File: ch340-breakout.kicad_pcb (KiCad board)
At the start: 2 copper layers, 31.8 x 28.9 mm, 20 parts, among them J1 USB_B_Mini, J2 Conn_01x08_Male, J3 Conn_02x05_Odd_Even, U1 SPX3819M5-L-3-3, U2 USBLC6-2SC6, U3 CH340G, Y1 12Mhz

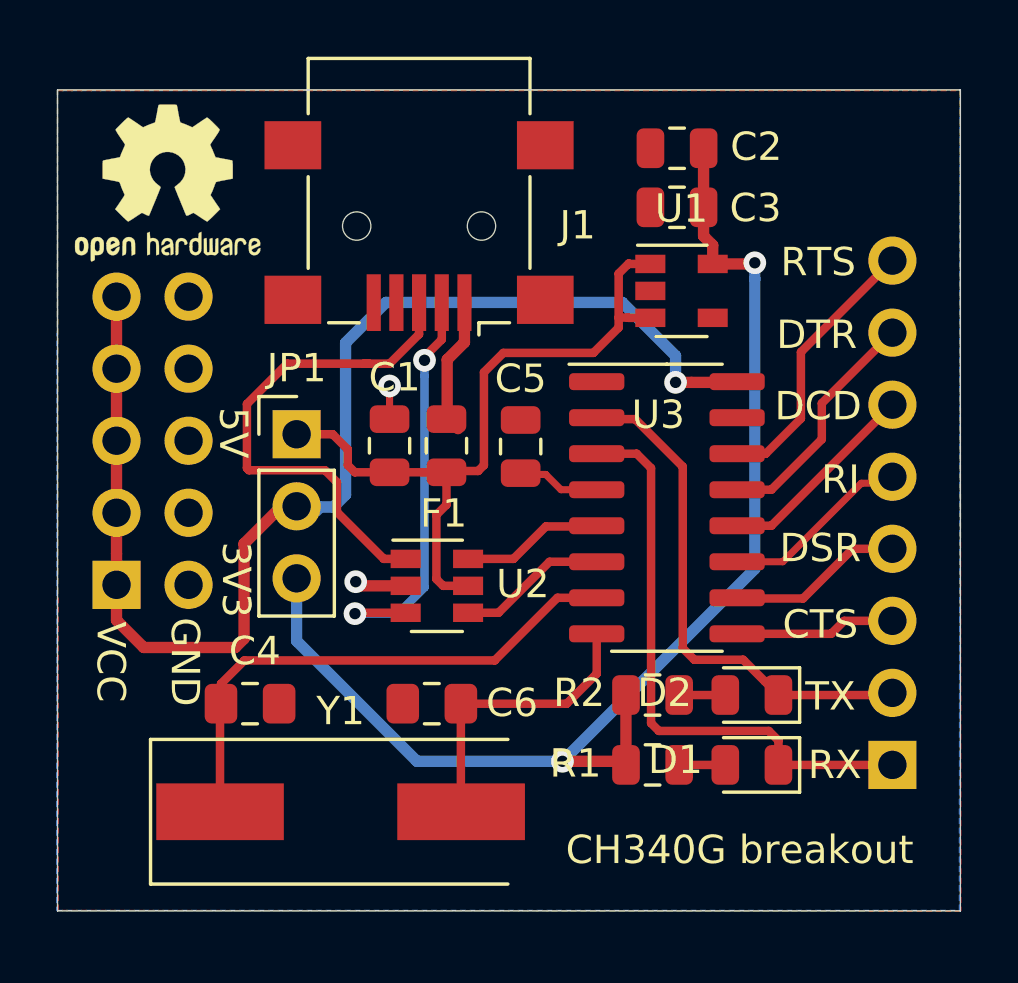
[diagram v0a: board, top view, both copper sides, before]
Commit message: finalizing and add power on led
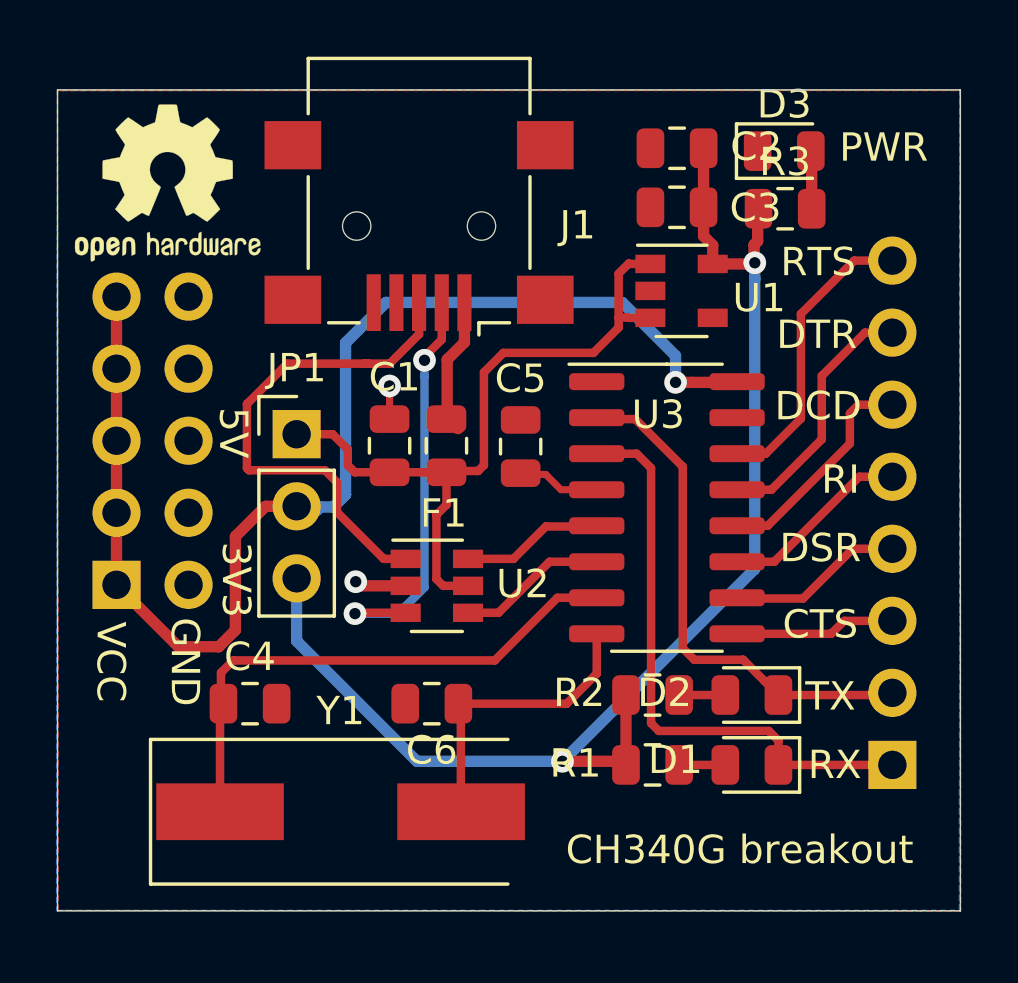
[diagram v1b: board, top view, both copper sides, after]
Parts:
- added D3: LED GREEN, LED_SMD:LED_0805_2012Metric, F.Cu at (166.3, 60.6)
- added R3: 100, Resistor_SMD:R_0805_2012Metric, F.Cu at (166.3, 62.6)
- C4, C6: footprint Capacitor_SMD:C_0805_2012Metric_Pad1.15x1.40mm_HandSolder -> Capacitor_SMD:C_0805_2012Metric
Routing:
- net Net-(D3-Pad2): track 0.00 -> 2.04 mm
- net +3V3: track 44.5 -> 46.5 mm
- net VCC: track 44.8 -> 43.8 mm
- net CH_RTS: track 9.67 -> 10.5 mm
- net CH_DCD: track 7.24 -> 7.87 mm
- net CH_DTR: track 7.88 -> 8.44 mm
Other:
- board text added: "$$version"
- board text added: "PWR"
- board text added: "https://820labs.net/ projects/ch340-breakout"

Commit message: silkscreen tweaks
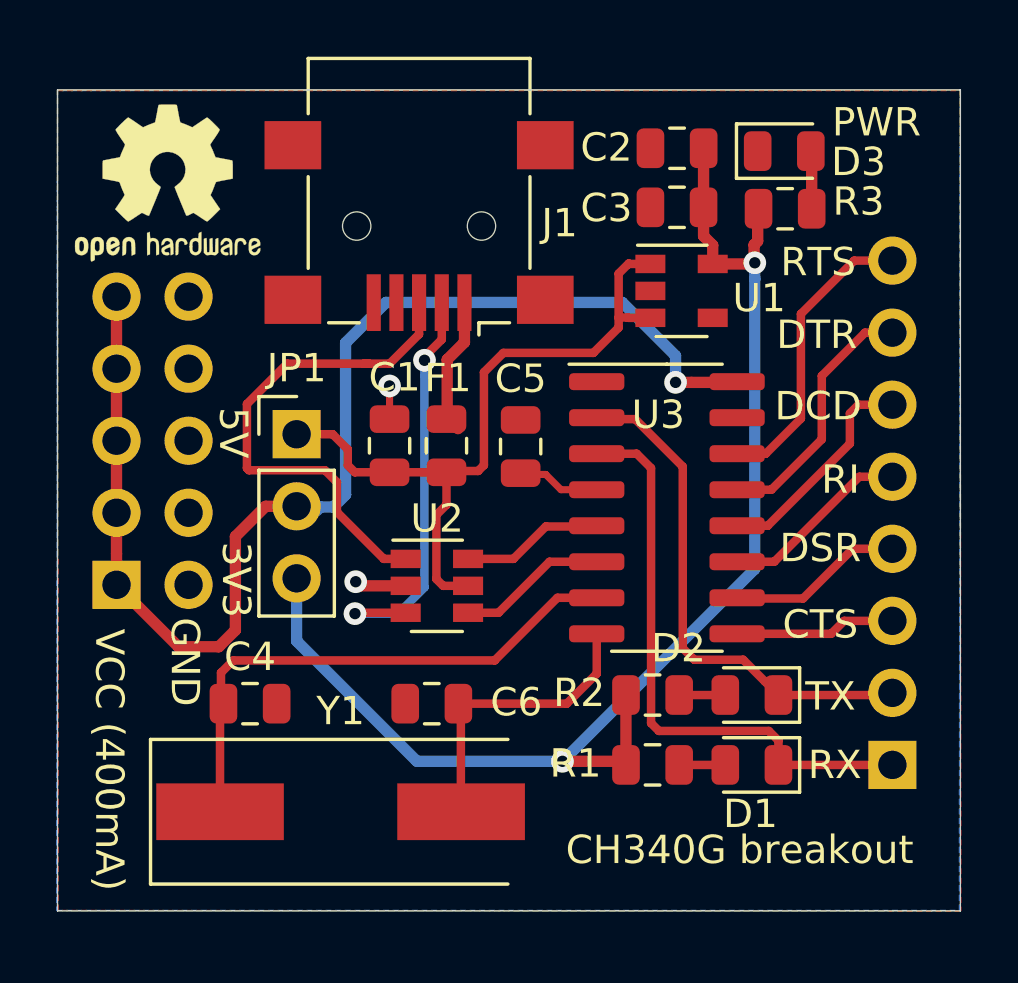
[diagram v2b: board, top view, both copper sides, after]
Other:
- board text added: "VCC (400mA)"
- board text removed: "VCC"
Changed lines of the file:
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@@
     (tags resistor)
     (attr smd)
-    (fp_text reference R3 (at 0 -1.65) (layer F.SilkS)
+    (fp_text reference R3 (at 2.5885 -0.254) (layer F.SilkS)
       (effects (font (size 1 1) (thickness 0.15)))
     )
@@
     (tags diode)
     (attr smd)
-    (fp_text reference D3 (at 0 -1.65) (layer F.SilkS)
+    (fp_text reference D3 (at 2.6185 0.381) (layer F.SilkS)
       (effects (font (size 1 1) (thickness 0.15)))
     )
@@
     (tags capacitor)
     (attr smd)
-    (fp_text reference C6 (at 0 -1.65) (layer F.SilkS)
+    (fp_text reference C6 (at -2.9808 0.0508) (layer F.SilkS)
       (effects (font (size 1 1) (thickness 0.15)))
     )
@@
     (tags resistor)
     (attr smd)
-    (fp_text reference F1 (at -2.3899 -0.1016 180) (layer F.SilkS)
+    (fp_text reference F1 (at 2.3853 0.0508 180) (layer F.SilkS)
       (effects (font (size 1 1) (thickness 0.15)))
     )
@@
     (tags capacitor)
     (attr smd)
-    (fp_text reference C3 (at -2.7686 -0.0254) (layer F.SilkS)
+    (fp_text reference C3 (at 2.4892 -0.0254) (layer F.SilkS)
       (effects (font (size 1 1) (thickness 0.15)))
     )
@@
     (tags capacitor)
     (attr smd)
-    (fp_text reference C2 (at -2.7917 0.0508) (layer F.SilkS)
+    (fp_text reference C2 (at 2.4915 0.0254) (layer F.SilkS)
       (effects (font (size 1 1) (thickness 0.15)))
     )
@@
     (tags SOT-23-6)
     (attr smd)
-    (fp_text reference U2 (at 3.0304 -0.061) (layer F.SilkS)
+    (fp_text reference U2 (at 0.0078 -2.3724) (layer F.SilkS)
       (effects (font (size 1 1) (thickness 0.15)))
     )
@@
     (tags "USB USB_B USB_Mini connector")
     (attr smd)
-    (fp_text reference J1 (at -5.588 0.0254) (layer F.SilkS)
+    (fp_text reference J1 (at -4.953 0.1016) (layer F.SilkS)
       (effects (font (size 1 1) (thickness 0.15)))
     )
@@
     (tags diode)
     (attr smd)
-    (fp_text reference D2 (at 3.0734 0.0762) (layer F.SilkS)
+    (fp_text reference D2 (at 2.5885 1.651) (layer F.SilkS)
       (effects (font (size 1 1) (thickness 0.15)))
     )
@@
     (tags diode)
     (attr smd)
-    (fp_text reference D1 (at 2.6947 0.1778) (layer F.SilkS)
+    (fp_text reference D1 (at 0.0485 -1.7272) (layer F.SilkS)
       (effects (font (size 1 1) (thickness 0.15)))
     )
@@
     )
   )
-  (gr_text PWR (at 169.799 60.452) (layer F.SilkS)
+  (gr_text PWR (at 169.545 59.563) (layer F.SilkS)
     (effects (font (size 1 1) (thickness 0.25)))
   )
@@
     (effects (font (size 1 1) (thickness 0.25)))
   )
-  (gr_text VCC (at 142.5448 78.5876 270) (layer F.SilkS)
+  (gr_text "VCC (400mA)" (at 142.494 82.042 270) (layer F.SilkS)
     (effects (font (size 1 1) (thickness 0.25)))
   )

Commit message: prepare for publishing: fixing LED resistor values, archive footprints, add missing data sheets
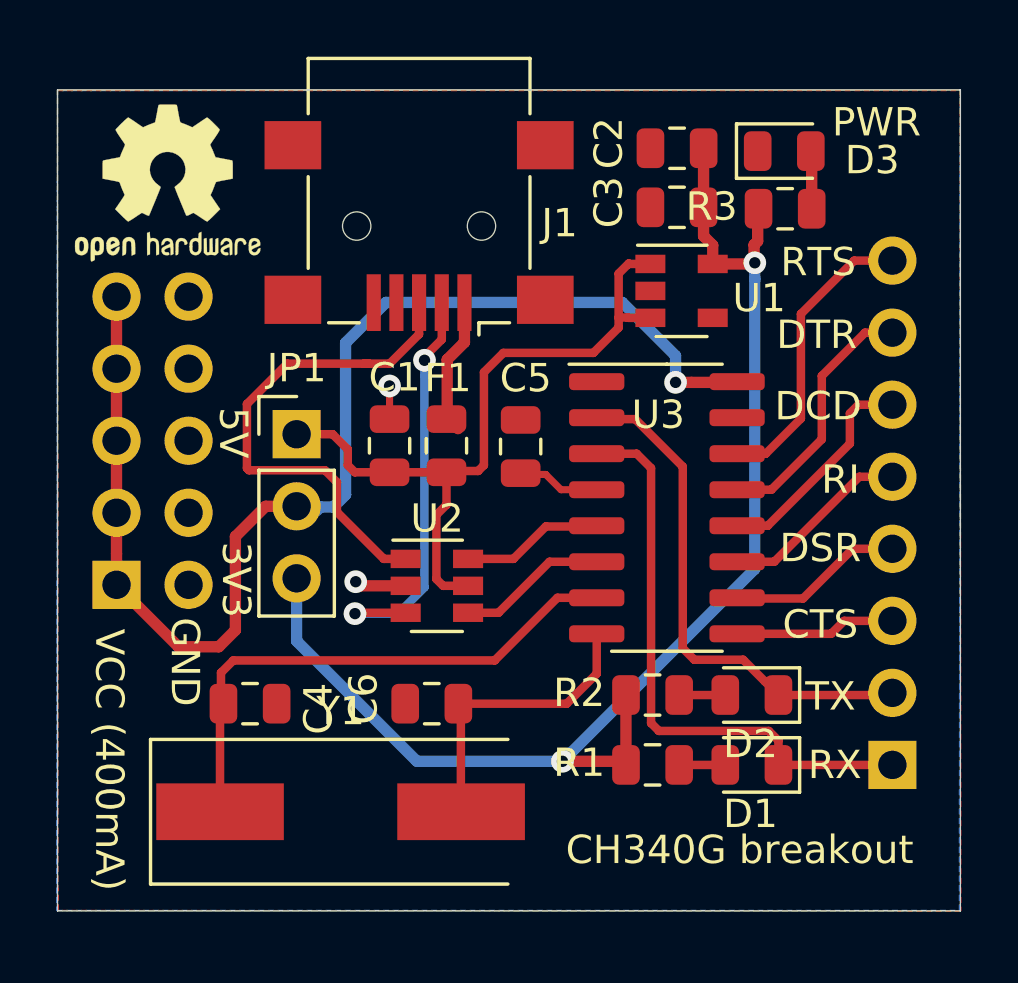
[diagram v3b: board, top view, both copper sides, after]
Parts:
- C1, C2, C3, C4, C5, C6: footprint Capacitor_SMD:C_0805_2012Metric -> ch340-breakout:C_0805_2012Metric
- D1, D2, D3: footprint LED_SMD:LED_0805_2012Metric -> ch340-breakout:LED_0805_2012Metric
- F1: footprint Fuse:Fuse_0805_2012Metric -> ch340-breakout:Fuse_0805_2012Metric
- J1: footprint Connector_USB:USB_Mini-B_Lumberg_2486_01_Horizontal -> ch340-breakout:USB_Mini-B_Lumberg_2486_01_Horizontal
- J2: footprint Connector_PinHeader_2.54mm:PinHeader_1x08_P2.54mm_Vertical -> ch340-breakout:PinHeader_1x08_P2.54mm_Vertical
- J3: footprint Connector_PinHeader_2.54mm:PinHeader_2x05_P2.54mm_Vertical -> ch340-breakout:PinHeader_2x05_P2.54mm_Vertical
- JP1: footprint Connector_PinHeader_2.54mm:PinHeader_1x03_P2.54mm_Vertical -> ch340-breakout:PinHeader_1x03_P2.54mm_Vertical
- R1, R3: value 100 -> 3K3; footprint Resistor_SMD:R_0805_2012Metric -> ch340-breakout:R_0805_2012Metric
- R2: value 100 -> 2K2; footprint Resistor_SMD:R_0805_2012Metric -> ch340-breakout:R_0805_2012Metric
- U1: footprint Package_TO_SOT_SMD:SOT-23-5 -> ch340-breakout:SOT-23-5
- U2: footprint Package_TO_SOT_SMD:SOT-23-6 -> ch340-breakout:SOT-23-6
- U3: footprint Package_SO:SOIC-16_3.9x9.9mm_P1.27mm -> ch340-breakout:SOIC-16_3.9x9.9mm_P1.27mm
- Y1: footprint Crystal:Crystal_SMD_HC49-SD -> ch340-breakout:Crystal_SMD_HC49-SD
